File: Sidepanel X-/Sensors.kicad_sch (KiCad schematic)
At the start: 8 parts, among them IC1 TMP112AQDRLRQ1, U1 GUVA-C32SM

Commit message: Paar Fehler behoben, Z+ no MOSFET
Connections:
- net VBAT is gone; now on net +3V3: C1.1, U1.4 (VCC)
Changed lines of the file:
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@@
   (junction (at 165.1 46.99) (diameter 0) (color 0 0 0 0)
+  )
+  (junction (at 50.8 34.29) (diameter 0) (color 0 0 0 0)
   )
   (junction (at 50.8 41.91) (diameter 0) (color 0 0 0 0)
@@
     (stroke (width 0) (type default) (color 0 0 0 0))
   )
-  (wire (pts (xy 48.26 46.99) (xy 50.8 46.99))
+  (wire (pts (xy 165.1 45.72) (xy 165.1 46.99))
     (stroke (width 0) (type default) (color 0 0 0 0))
   )
-  (wire (pts (xy 165.1 45.72) (xy 165.1 46.99))
+  (wire (pts (xy 29.21 34.29) (xy 50.8 34.29))
     (stroke (width 0) (type default) (color 0 0 0 0))
   )
@@
     (stroke (width 0) (type default) (color 0 0 0 0))
   )
-  (wire (pts (xy 50.8 33.02) (xy 50.8 35.56))
+  (wire (pts (xy 50.8 33.02) (xy 50.8 34.29))
     (stroke (width 0) (type default) (color 0 0 0 0))
   )
@@
   )
   (wire (pts (xy 165.1 46.99) (xy 157.48 46.99))
+    (stroke (width 0) (type default) (color 0 0 0 0))
+  )
+  (wire (pts (xy 29.21 46.99) (xy 50.8 46.99))
+    (stroke (width 0) (type default) (color 0 0 0 0))
+  )
+  (wire (pts (xy 50.8 34.29) (xy 50.8 35.56))
     (stroke (width 0) (type default) (color 0 0 0 0))
   )
@@
     (stroke (width 0) (type default) (color 0 0 0 0))
   )
+  (wire (pts (xy 29.21 46.99) (xy 29.21 34.29))
+    (stroke (width 0) (type default) (color 0 0 0 0))
+  )
   (wire (pts (xy 69.85 41.91) (xy 71.12 41.91))
     (stroke (width 0) (type default) (color 0 0 0 0))
@@
     (stroke (width 0) (type default) (color 0 0 0 0))
   )
-  (hierarchical_label "VBAT" (shape input) (at 48.26 46.99 180)
-    (effects (font (size 1.27 1.27)) (justify right))
-  )
-  (hierarchical_label "VBAT" (shape input) (at 48.26 46.99 180)
-    (effects (font (size 1.27 1.27)) (justify right))
-  )
   (hierarchical_label "SDA_TMP" (shape bidirectional) (at 166.37 46.99 0)

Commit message: Fixed some DRC errors.
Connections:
- net GND: now also IC1.3 (ALERT)
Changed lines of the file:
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@@
   (junction (at 165.1 39.37) (diameter 0) (color 0 0 0 0)
   )
+  (junction (at 124.46 46.99) (diameter 0) (color 0 0 0 0)
+  )
   (junction (at 71.12 41.91) (diameter 0) (color 0 0 0 0)
   )
@@
     (stroke (width 0) (type default) (color 0 0 0 0))
   )
-  (wire (pts (xy 124.46 44.45) (xy 124.46 48.26))
+  (wire (pts (xy 124.46 46.99) (xy 124.46 48.26))
+    (stroke (width 0) (type default) (color 0 0 0 0))
+  )
+  (wire (pts (xy 124.46 44.45) (xy 124.46 46.99))
+    (stroke (width 0) (type default) (color 0 0 0 0))
+  )
+  (wire (pts (xy 127 46.99) (xy 124.46 46.99))
     (stroke (width 0) (type default) (color 0 0 0 0))
   )
@@
   )
   (symbol (lib_id "USER_Optic:GUVA-C32SM") (at 60.96 44.45 180) (unit 1)
-    (in_bom yes) (on_board yes) (fields_autoplaced)
-    (property "Reference" "U1" (id 0) (at 60.96 34.29 0))
-    (property "Value" "GUVA-C32SM" (id 1) (at 60.96 36.83 0))
-    (property "Footprint" "Package_SO:SO-4_4.4x3.6mm_P2.54mm" (id 2) (at 60.96 45.72 0)
-      (effects (font (size 1.27 1.27)) hide)
-    )
-    (property "Datasheet" "" (id 3) (at 60.96 45.72 0)
-      (effects (font (size 1.27 1.27)) hide)
-    )
+    (in_bom yes) (on_board yes)
+    (property "Reference" "U1" (id 0) (at 60.96 54.61 0))
+    (property "Value" "GUVA-C32SM" (id 1) (at 60.96 52.07 0))
+    (property "Footprint" "Package_SO:SO-4_4.4x3.6mm_P2.54mm" (id 2) (at 59.69 25.146 0))
+    (property "Datasheet" "" (id 3) (at 60.96 43.18 0)
+      (effects (font (size 1.27 1.27)) hide)
+    )

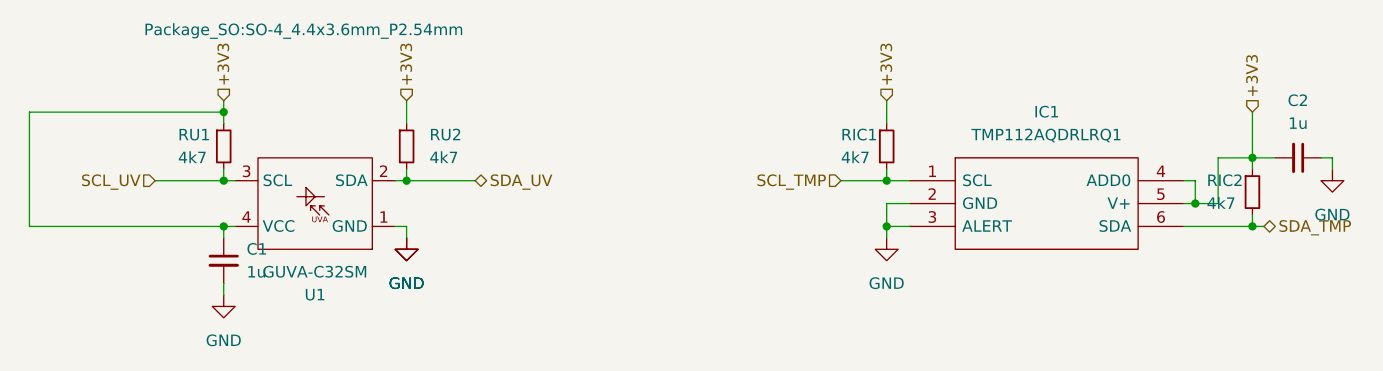
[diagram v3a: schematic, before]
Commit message: Adjusted the panel naming so that it conforms to the coordinate system convention governed by the Cubesat Design Specification.
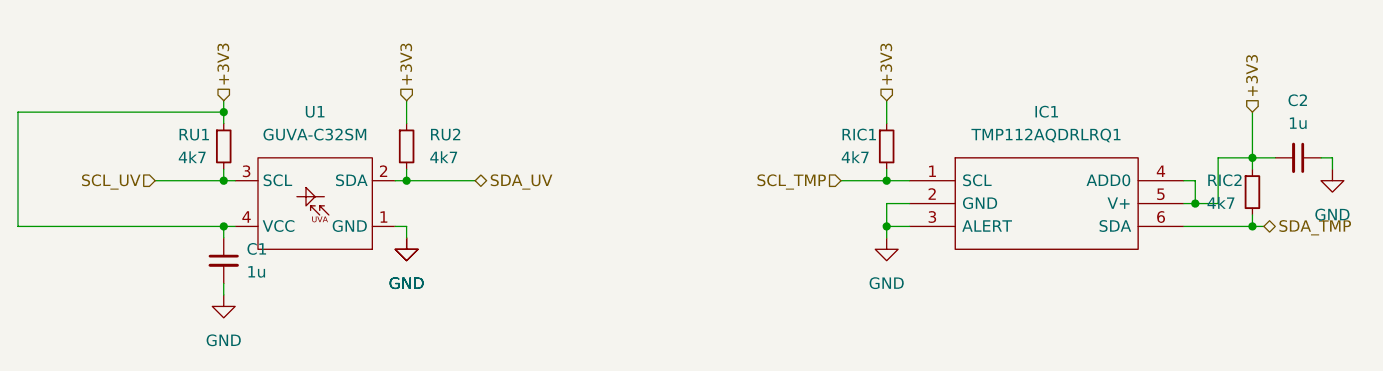
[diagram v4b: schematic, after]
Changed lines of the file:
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@@
   (junction (at 124.46 46.99) (diameter 0) (color 0 0 0 0)
   )
+  (junction (at 50.8 34.29) (diameter 0) (color 0 0 0 0)
+  )
   (junction (at 71.12 41.91) (diameter 0) (color 0 0 0 0)
   )
@@
   (junction (at 165.1 46.99) (diameter 0) (color 0 0 0 0)
   )
-  (junction (at 50.8 34.29) (diameter 0) (color 0 0 0 0)
-  )
   (junction (at 50.8 41.91) (diameter 0) (color 0 0 0 0)
   )
@@
     (stroke (width 0) (type default) (color 0 0 0 0))
   )
+  (wire (pts (xy 27.94 46.99) (xy 50.8 46.99))
+    (stroke (width 0) (type default) (color 0 0 0 0))
+  )
   (wire (pts (xy 165.1 45.72) (xy 165.1 46.99))
     (stroke (width 0) (type default) (color 0 0 0 0))
   )
-  (wire (pts (xy 29.21 34.29) (xy 50.8 34.29))
+  (wire (pts (xy 50.8 34.29) (xy 50.8 35.56))
+    (stroke (width 0) (type default) (color 0 0 0 0))
+  )
+  (wire (pts (xy 124.46 46.99) (xy 124.46 48.26))
     (stroke (width 0) (type default) (color 0 0 0 0))
   )
@@
     (stroke (width 0) (type default) (color 0 0 0 0))
   )
+  (wire (pts (xy 27.94 46.99) (xy 27.94 34.29))
+    (stroke (width 0) (type default) (color 0 0 0 0))
+  )
   (wire (pts (xy 71.12 41.91) (xy 78.74 41.91))
     (stroke (width 0) (type default) (color 0 0 0 0))
@@
     (stroke (width 0) (type default) (color 0 0 0 0))
   )
+  (wire (pts (xy 27.94 34.29) (xy 50.8 34.29))
+    (stroke (width 0) (type default) (color 0 0 0 0))
+  )
   (wire (pts (xy 119.38 41.91) (xy 124.46 41.91))
     (stroke (width 0) (type default) (color 0 0 0 0))
@@
     (stroke (width 0) (type default) (color 0 0 0 0))
   )
-  (wire (pts (xy 29.21 46.99) (xy 50.8 46.99))
-    (stroke (width 0) (type default) (color 0 0 0 0))
-  )
-  (wire (pts (xy 50.8 34.29) (xy 50.8 35.56))
+  (wire (pts (xy 124.46 46.99) (xy 127 46.99))
     (stroke (width 0) (type default) (color 0 0 0 0))
   )
@@
     (stroke (width 0) (type default) (color 0 0 0 0))
   )
-  (wire (pts (xy 29.21 46.99) (xy 29.21 34.29))
-    (stroke (width 0) (type default) (color 0 0 0 0))
-  )
   (wire (pts (xy 69.85 41.91) (xy 71.12 41.91))
     (stroke (width 0) (type default) (color 0 0 0 0))
@@
     (stroke (width 0) (type default) (color 0 0 0 0))
   )
-  (wire (pts (xy 124.46 46.99) (xy 124.46 48.26))
-    (stroke (width 0) (type default) (color 0 0 0 0))
-  )
   (wire (pts (xy 124.46 44.45) (xy 124.46 46.99))
-    (stroke (width 0) (type default) (color 0 0 0 0))
-  )
-  (wire (pts (xy 127 46.99) (xy 124.46 46.99))
     (stroke (width 0) (type default) (color 0 0 0 0))
   )
@@
   )
   (symbol (lib_id "USER_Optic:GUVA-C32SM") (at 60.96 44.45 180) (unit 1)
-    (in_bom yes) (on_board yes)
-    (property "Reference" "U1" (id 0) (at 60.96 54.61 0))
-    (property "Value" "GUVA-C32SM" (id 1) (at 60.96 52.07 0))
-    (property "Footprint" "Package_SO:SO-4_4.4x3.6mm_P2.54mm" (id 2) (at 59.69 25.146 0))
-    (property "Datasheet" "" (id 3) (at 60.96 43.18 0)
-      (effects (font (size 1.27 1.27)) hide)
-    )
+    (in_bom yes) (on_board yes) (fields_autoplaced)
+    (property "Reference" "U1" (id 0) (at 60.96 34.29 0))
+    (property "Value" "GUVA-C32SM" (id 1) (at 60.96 36.83 0))
+    (property "Footprint" "Package_SO:SO-4_4.4x3.6mm_P2.54mm" (id 2) (at 60.96 45.72 0)
+      (effects (font (size 1.27 1.27)) hide)
+    )
+    (property "Datasheet" "" (id 3) (at 60.96 45.72 0)
+      (effects (font (size 1.27 1.27)) hide)
+    )
